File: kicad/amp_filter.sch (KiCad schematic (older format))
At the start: 10 parts, among them M1 2N7000

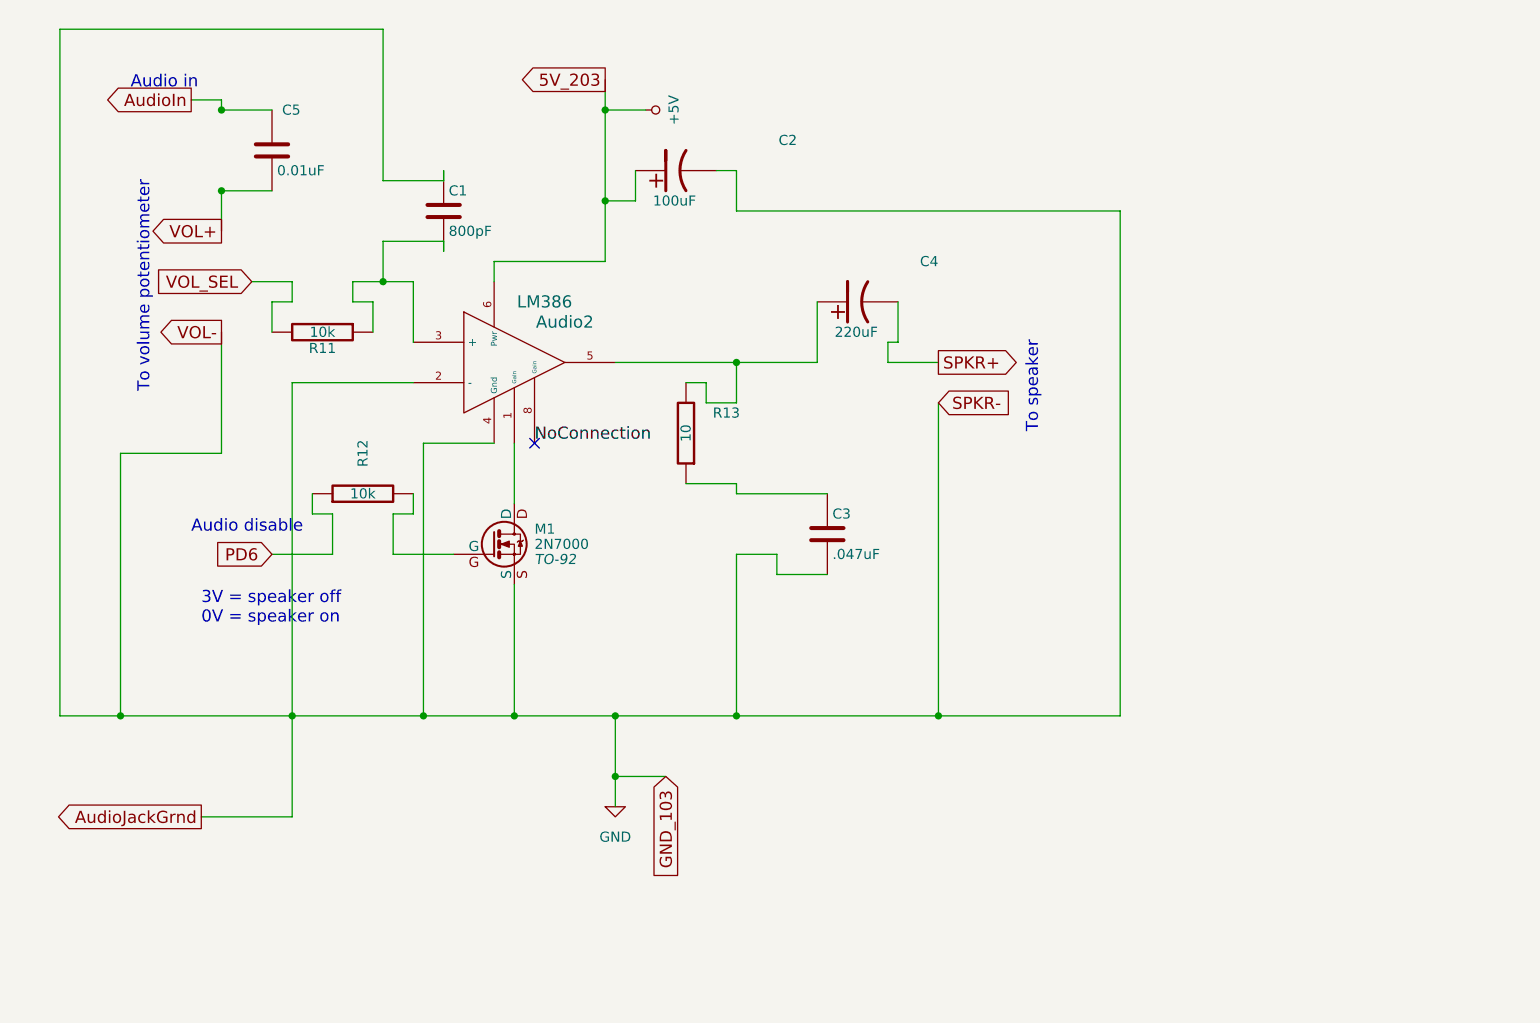
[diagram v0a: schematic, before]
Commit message: Final routing
Removed some intermediary routing steps, too
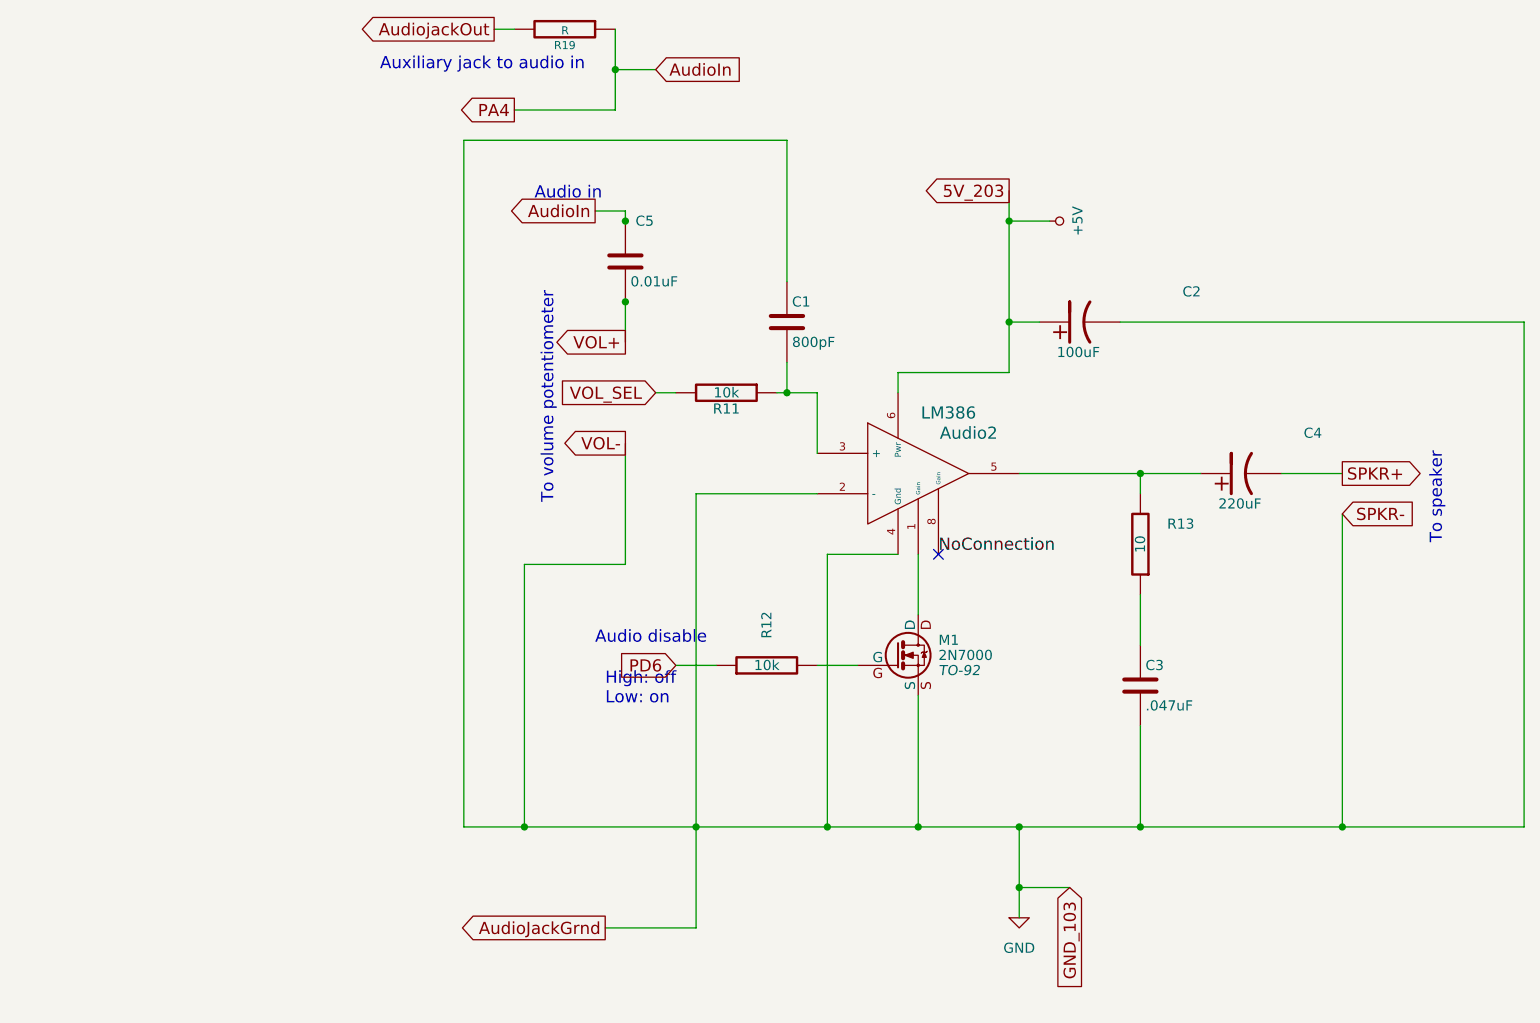
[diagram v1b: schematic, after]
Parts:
- added R19: R, ~, symbol R
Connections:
- net AudioIn: now also R19.1
- new net AudiojackOut: R19.2
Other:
- note added: "Auxiliary jack to audio in"
- note added: "High: off\nLow: on"
- note removed: "3V = speaker off\n0V = speaker on"
- moved on the sheet: Audio2, C1, C2, C3, C4, C5, M1, R11, R12, R13
